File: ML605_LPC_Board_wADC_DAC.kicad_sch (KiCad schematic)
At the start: 25 parts, among them J1 ASP-134604-01, J10 Conn_02x06_Odd_Even, J11 Conn_02x06_Odd_Even, J12 Conn_02x06_Odd_Even, J2 Conn_01x03_Pin, J3 Conn_01x03_Pin, U1 LMV7219M7, U2 LMV7219M7, U3 NCV317

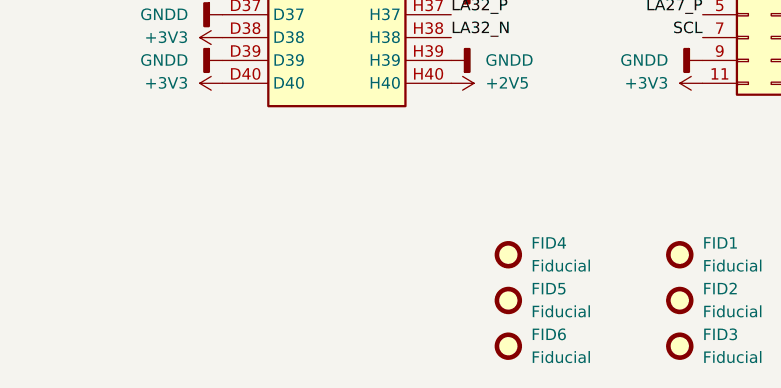
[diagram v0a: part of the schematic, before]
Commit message: Rev 1.1
Multiple changes are made, as per suggestions made by the redditors of r/PrintedCircuitBoards. Firstly, two 50 ohm resistors were added in series with the DAC output in order to comply with the minimum peak output current of the op-amps of 50mA. Secondly, two M3 mounting holes were added in order to have the possibility to add standoffs. Thirdly, a clearance issue regarding jumpers near the LPC connector on the ML602 board was fixed by changing the board geometry to include a cutout for these.

Some other things to look into are the use of some ferrite beads for supplies of the analog ICs.
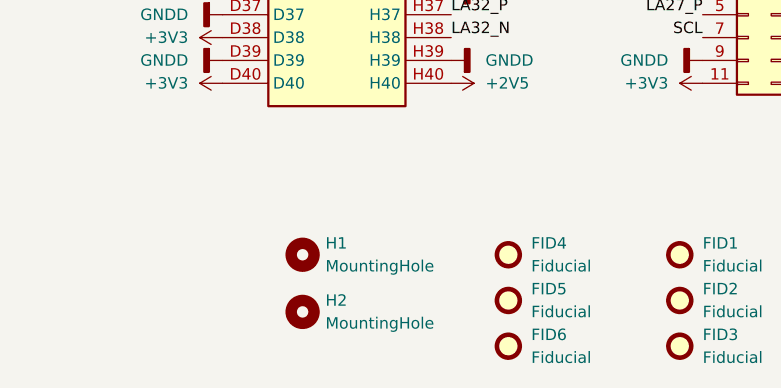
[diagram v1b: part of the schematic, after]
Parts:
- added H1, H2: MountingHole, MountingHole:MountingHole_3.2mm_M3, symbol Mechanical:MountingHole
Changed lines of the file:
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@@
 	)
 	(symbol
+		(lib_id "Mechanical:MountingHole")
+		(at 41.91 242.57 0)
+		(unit 1)
+		(exclude_from_sim no)
+		(in_bom yes)
+		(on_board yes)
+		(dnp no)
+		(fields_autoplaced yes)
+		(property "Reference" "H1"
+			(at 44.45 241.2999 0)
+			(effects
+				(font
+					(size 1.27 1.27)
+				)
+				(justify left)
+			)
+		)
+		(property "Value" "MountingHole"
+			(at 44.45 243.8399 0)
+			(effects
+				(font
+					(size 1.27 1.27)
+				)
+				(justify left)
+			)
+		)
+		(property "Footprint" "MountingHole:MountingHole_3.2mm_M3"
+			(at 41.91 242.57 0)
+			(effects
+				(font
+					(size 1.27 1.27)
+				)
+				(hide yes)
+			)
+		)
+		(property "Datasheet" "~"
+			(at 41.91 242.57 0)
+			(effects
+				(font
+					(size 1.27 1.27)
+				)
+				(hide yes)
+			)
+		)
+		(property "Description" "Mounting Hole without connection"
+			(at 41.91 242.57 0)
+			(effects
+				(font
+					(size 1.27 1.27)
+				)
+				(hide yes)
+			)
+		)
+		(instances
+			(project "ML605_LPC_Board_wADC_DAC"
+				(path "/35bdcd8d-8b21-4a24-9357-7d92e5ad0993"
+					(reference "H1")
+					(unit 1)
+				)
+			)
+		)
+	)
+	(symbol
 		(lib_id "power:+3V3")
 		(at 33.02 203.2 90)
@@
 					(unit 1)
 				)
+			)
+		)
+	)
+	(symbol
+		(lib_id "Mechanical:MountingHole")
+		(at 41.91 248.92 0)
+		(unit 1)
+		(exclude_from_sim no)
+		(in_bom yes)
+		(on_board yes)
+		(dnp no)
+		(fields_autoplaced yes)
+		(property "Reference" "H2"
+			(at 44.45 247.6499 0)
+			(effects
+				(font
+					(size 1.27 1.27)
+				)
+				(justify left)
+			)
+		)
+		(property "Value" "MountingHole"
+			(at 44.45 250.1899 0)
+			(effects
+				(font
+					(size 1.27 1.27)
+				)
+				(justify left)
+			)
+		)
+		(property "Footprint" "MountingHole:MountingHole_3.2mm_M3"
+			(at 41.91 248.92 0)
+			(effects
+				(font
+					(size 1.27 1.27)
+				)
+				(hide yes)
+			)
+		)
+		(property "Datasheet" "~"
+			(at 41.91 248.92 0)
+			(effects
+				(font
+					(size 1.27 1.27)
+				)
+				(hide yes)
+			)
+		)
+		(property "Description" "Mounting Hole without connection"
+			(at 41.91 248.92 0)
+			(effects
+				(font
+					(size 1.27 1.27)
+				)
+				(hide yes)
+			)
+		)
+		(instances
+			(project "ML605_LPC_Board_wADC_DAC"
+				(path "/35bdcd8d-8b21-4a24-9357-7d92e5ad0993"
+					(reference "H2")
+					(unit 1)
+				)

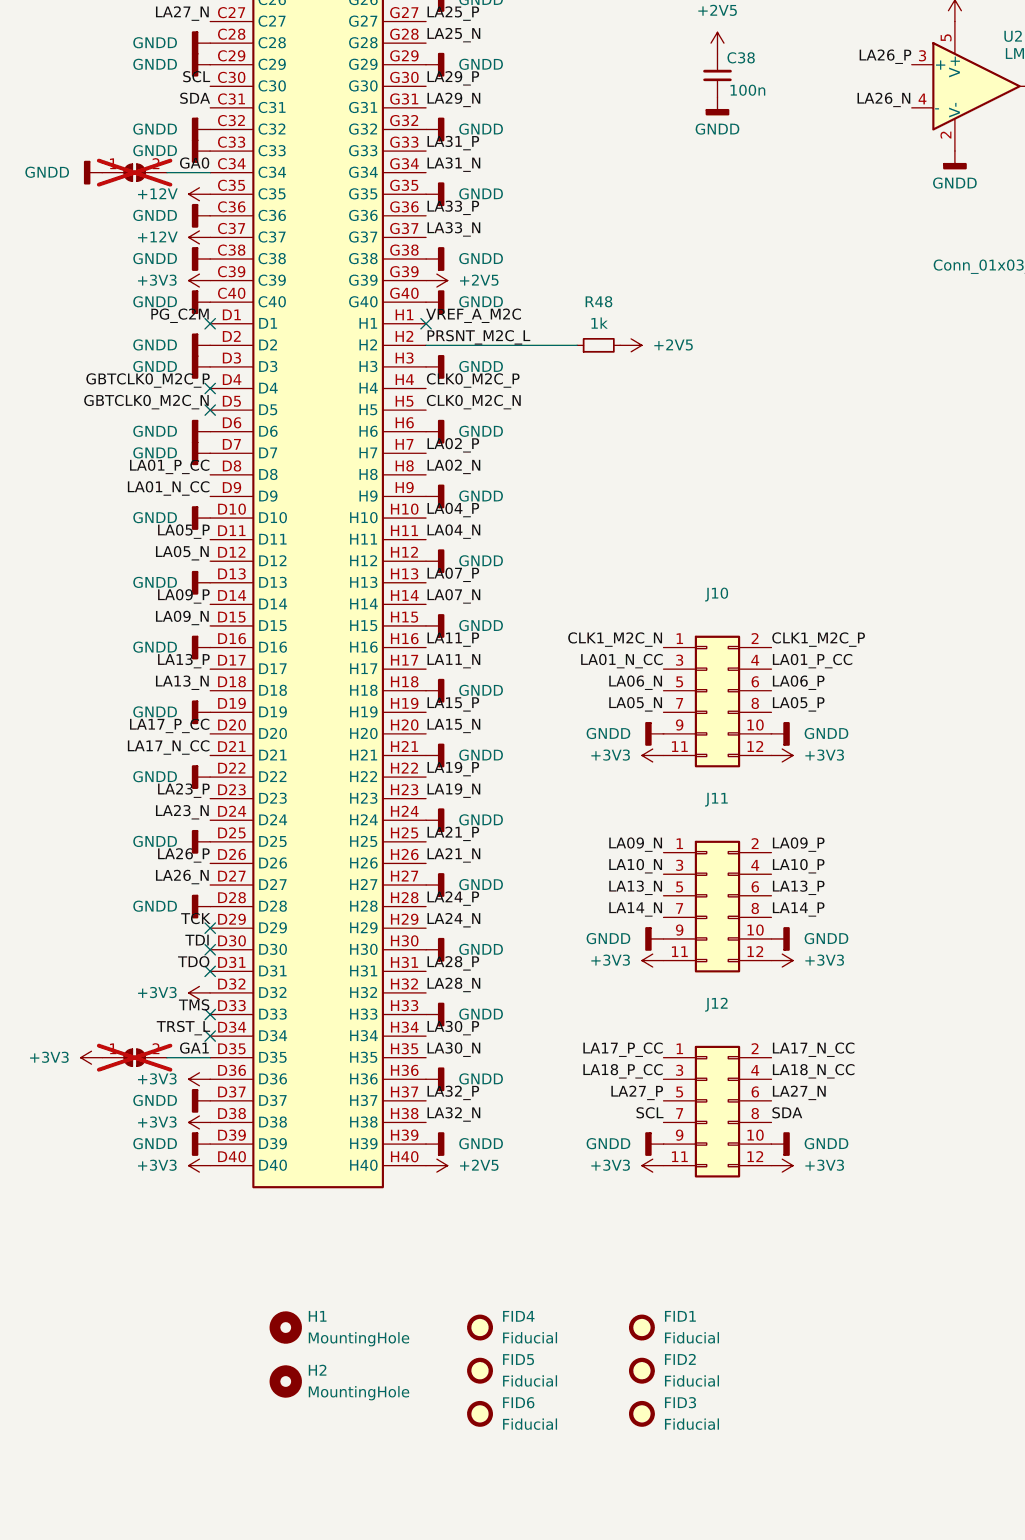
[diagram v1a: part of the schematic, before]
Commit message: Added identification EEPROM to comply with the 2019 revision of the VITA 57.1 standard
The EEPROM and its complementary components are marked as DNP, as they are not necessary for the ML602 board to function
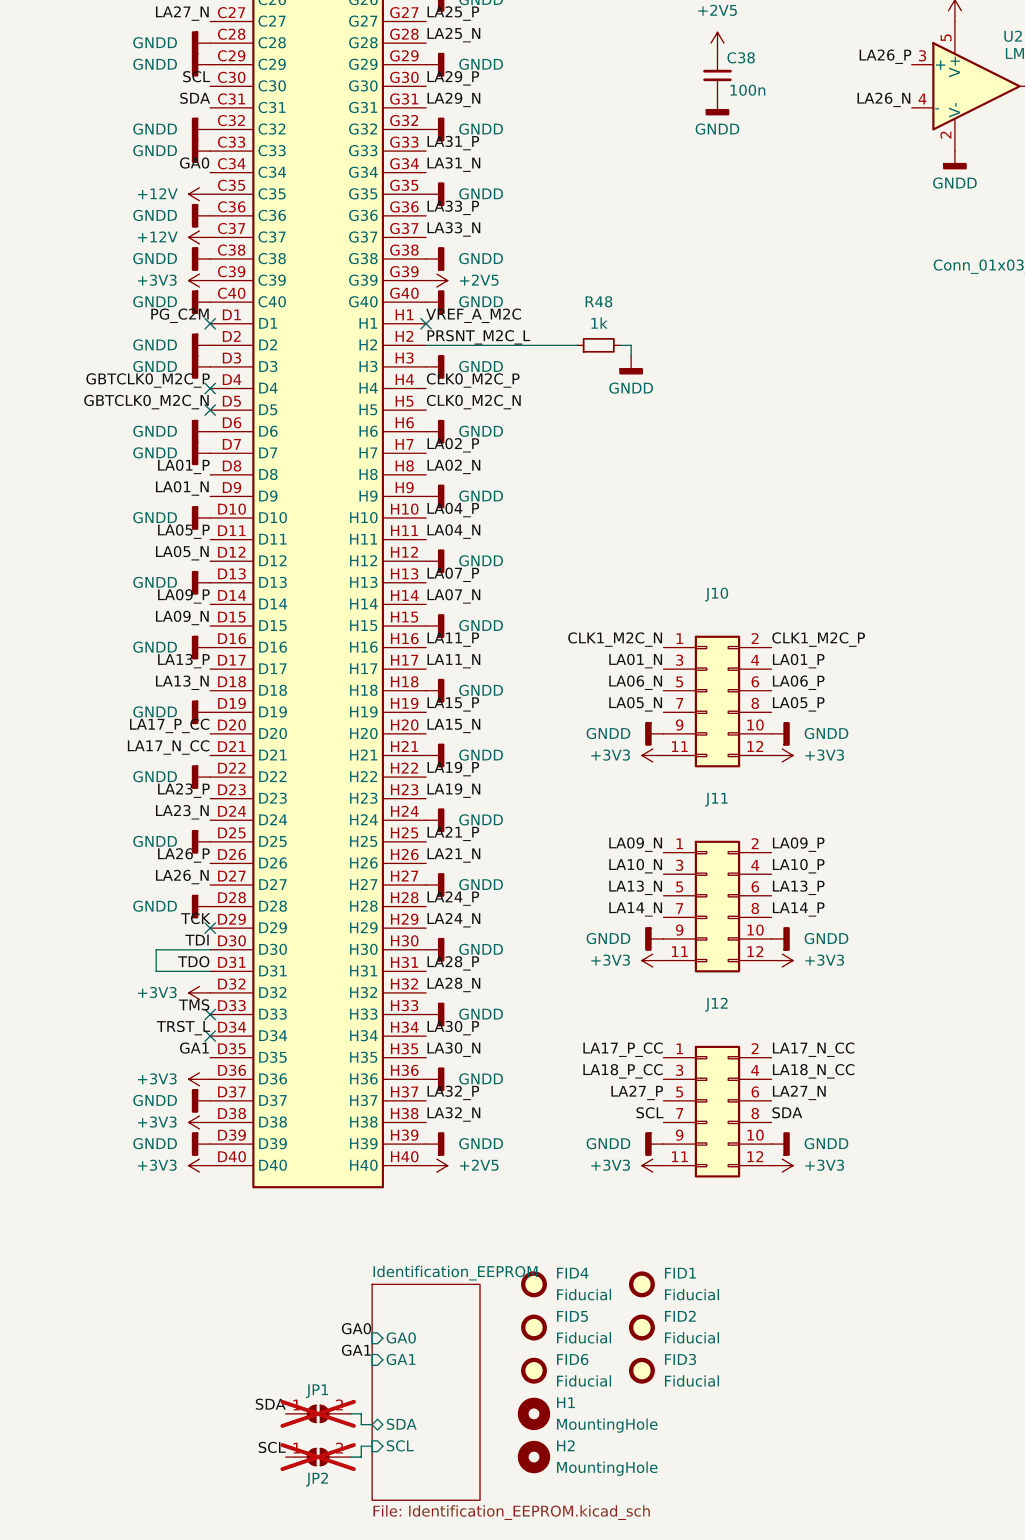
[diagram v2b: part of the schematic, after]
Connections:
- net TDO is gone; now on net TDI: J1.D31
- net +2V5: no longer R48.2
- net +3V3: no longer JP2.1 (A)
- net GA0: no longer JP1.2 (B)
- net GA1: no longer JP2.2 (B)
- net GNDA: now also R48.2; no longer JP1.1 (A)
- net SCL: now also JP2.1 (A)
- net SDA: now also JP1.1 (A)
- net LA01_N_CC renamed LA01_N
- net LA01_P_CC renamed LA01_P
- new net Identification_EEPROM/SCL: JP2.2 (B)
- new net Identification_EEPROM/SDA: JP1.2 (B)
- no-connect marks 13 -> 11
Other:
- added sheet Identification_EEPROM (Identification_EEPROM.kicad_sch)
- moved on the sheet: FID1, FID2, FID3, FID4, FID5, FID6, H1, H2

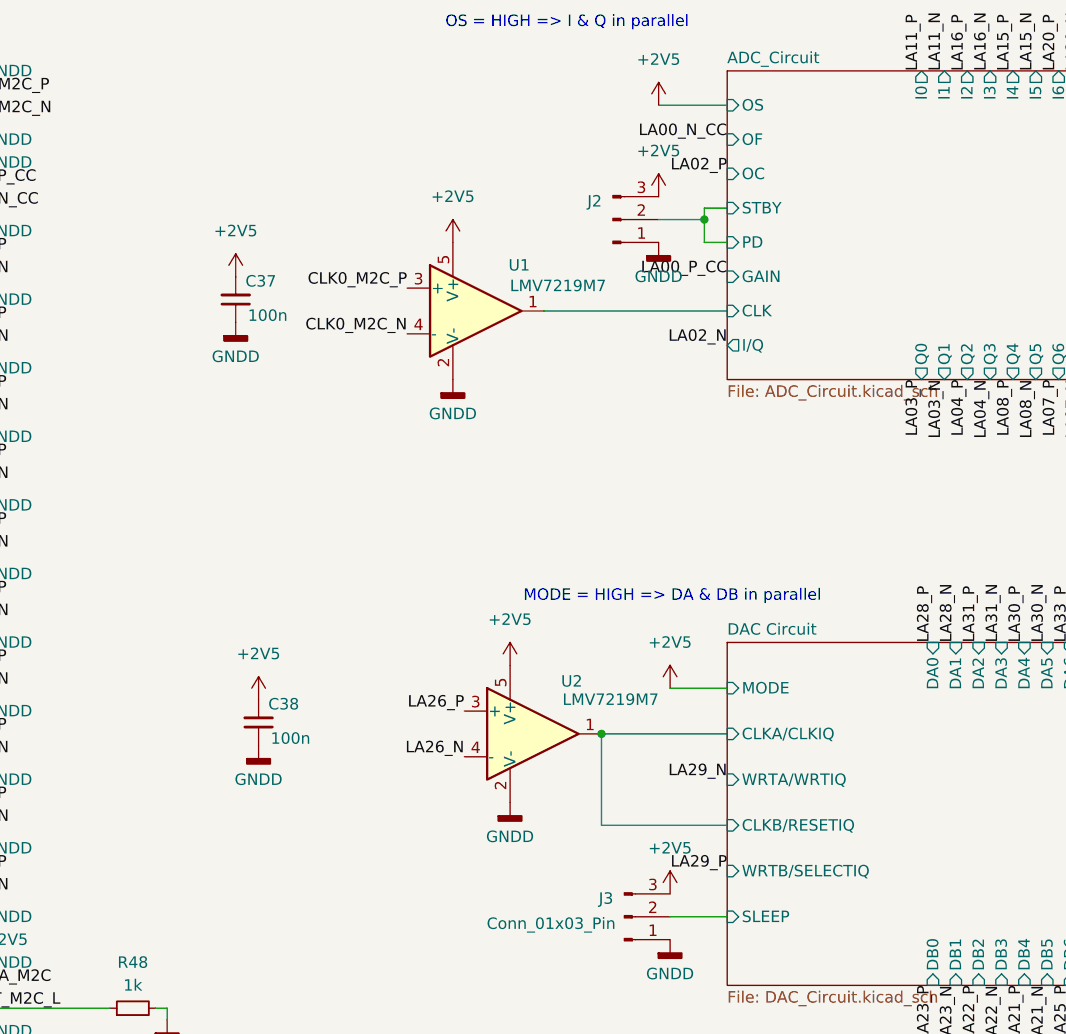
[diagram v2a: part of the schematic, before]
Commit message: Changed clock comparators to dedicated LVDS decoders and changed ADC Vdd inductor to ferrite bead
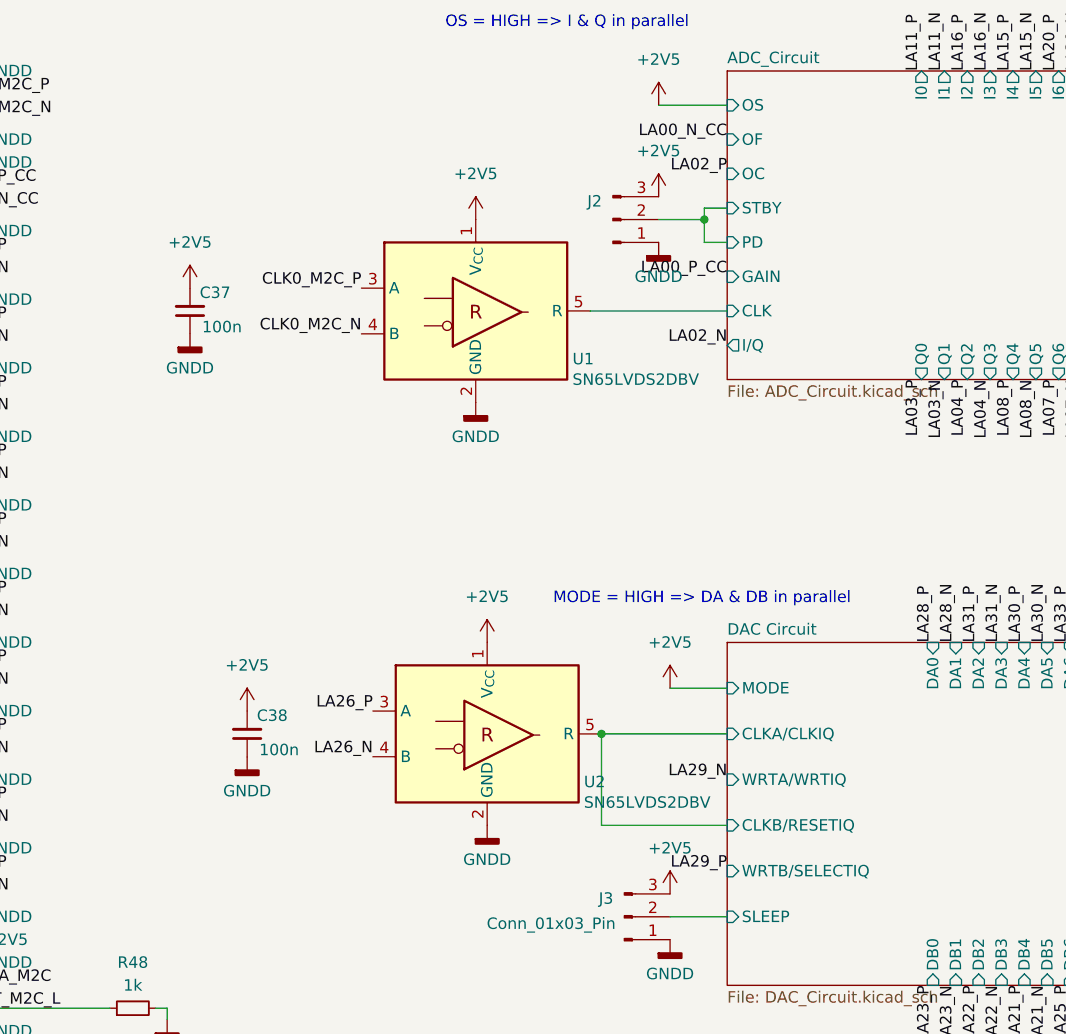
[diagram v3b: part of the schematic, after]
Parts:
- removed U1, U2: LMV7219M7, Package_TO_SOT_SMD:SOT-353_SC-70-5, symbol Comparator:LMV7219M7
- added U1, U2: SN65LVDS2DBV, Package_TO_SOT_SMD:SOT-23-5, symbol Interface:SN65LVDS2DBV
- H1, H2: Mouser Link (none) -> N/A
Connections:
- net +2V5: now also U1.1 (V_{CC}), U2.1 (V_{CC})
- net ADC_Circuit/CLK: now also U1.5 (R)
- net CLK0_M2C_N: now also U1.4 (B)
- net CLK0_M2C_P: now also U1.3 (A)
- net DAC Circuit/CLKA/CLKIQ: now also U2.5 (R)
- net GNDA: now also U1.2 (GND), U2.2 (GND)
- net LA26_N: now also U2.4 (B)
- net LA26_P: now also U2.3 (A)
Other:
- moved on the sheet: C37, C38

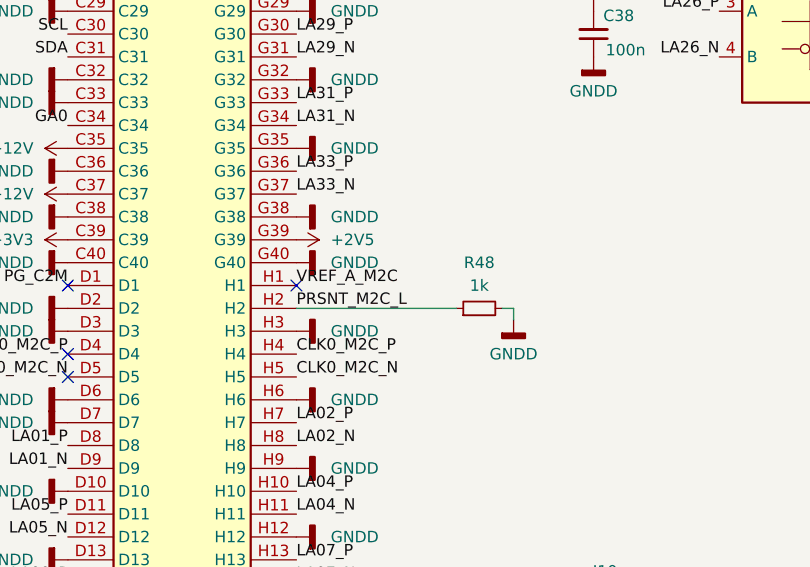
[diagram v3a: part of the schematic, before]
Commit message: Tied PRSNT pin directly to ground without resistor, fixed reference of J1
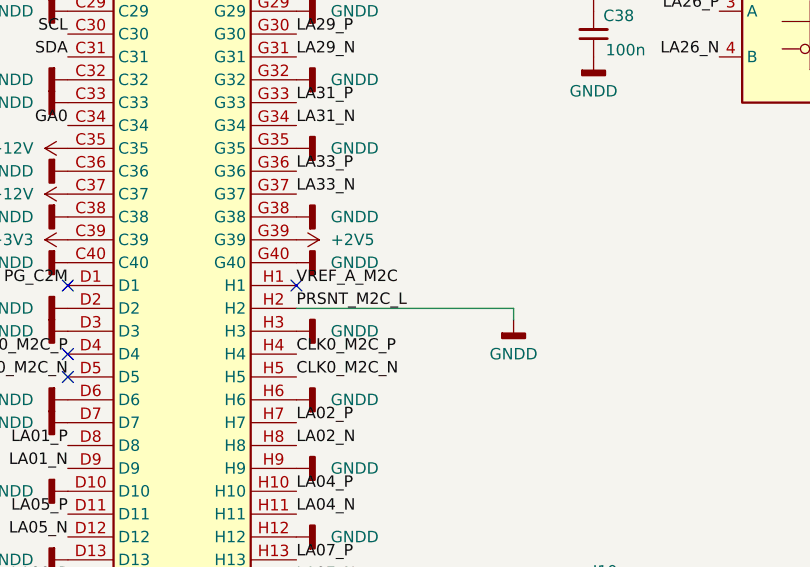
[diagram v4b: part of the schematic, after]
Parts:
- removed R48: 1k, Resistor_SMD:R_0805_2012Metric_Pad1.20x1.40mm_HandSolder, symbol Device:R_Small
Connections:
- net PRSNT_M2C_L is gone; now on net GNDA: J1.H2
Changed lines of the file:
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@@
 	(wire
 		(pts
-			(xy 81.28 127) (xy 82.55 127)
-		)
-		(stroke
-			(width 0)
-			(type default)
-		)
-	)
-	(wire
-		(pts
 			(xy 137.16 26.67) (xy 144.78 26.67)
 		)
@@
 	(wire
 		(pts
-			(xy 58.42 127) (xy 76.2 127)
+			(xy 58.42 127) (xy 82.55 127)
 		)
 		(stroke
@@
 					(unit 1)
 				)
-			)
-		)
-	)
-	(symbol
-		(lib_id "Device:R_Small")
-		(at 78.74 127 90)
-		(unit 1)
-		(exclude_from_sim no)
-		(in_bom yes)
-		(on_board yes)
-		(dnp no)
-		(fields_autoplaced yes)
-		(property "Reference" "R48"
-			(at 78.74 121.92 90)
-			(effects
-				(font
-					(size 1.27 1.27)
-				)
-			)
-		)
-		(property "Value" "1k"
-			(at 78.74 124.46 90)
-			(effects
-				(font
-					(size 1.27 1.27)
-				)
-			)
-		)
-		(property "Footprint" "Resistor_SMD:R_0805_2012Metric_Pad1.20x1.40mm_HandSolder"
-			(at 78.74 127 0)
-			(effects
-				(font
-					(size 1.27 1.27)
-				)
-				(hide yes)
-			)
-		)
-		(property "Datasheet" "~"
-			(at 78.74 127 0)
-			(effects
-				(font
-					(size 1.27 1.27)
-				)
-				(hide yes)
-			)
-		)
-		(property "Description" "Resistor, small symbol"
-			(at 78.74 127 0)
-			(effects
-				(font
-					(size 1.27 1.27)
-				)
-				(hide yes)
-			)
-		)
-		(property "Mouser Link" "https://ro.mouser.com/ProductDetail/YAGEO/AC0805JR-071KL?qs=sGAEpiMZZMtlubZbdhIBIG07xJe44c5APYMj%2Fj7aA%2Fo%3D"
-			(at 78.74 127 0)
-			(effects
-				(font
-					(size 1.27 1.27)
-				)
-				(hide yes)
-			)
-		)
-		(pin "1"
-		)
-		(pin "2"
-		)
-		(instances
-			(project "ML605_LPC_Board_wADC_DAC"
-				(path "/35bdcd8d-8b21-4a24-9357-7d92e5ad0993"
-					(reference "R48")
-					(unit 1)
-				)
